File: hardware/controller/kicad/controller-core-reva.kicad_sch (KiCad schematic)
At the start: 187 parts, among them J101 12V_ISOLATED_INPUT / JST XH, J102 STM_SWD / 1x6 2.54mm, J103 ESP_UART / 1x6 2.54mm, J104 UI_LINK / IDC 2x8 2.54mm, J105 JP13 NTC / 2 vías, J106 JP5 FLOW ADAPTER / VCC-GND-OC, J107 JP14 DOOR / contacto seco, J108 JP16 VISUAL V1..V8 / XH-8, J109 JP22 WATER / RED-WHITE-BLACK, J110 USB-C SERVICE / USB 2.0, J111 USB BENCH POWER / OPEN, J112 24V_ACTUATOR_INPUT / JST XH, J113 JP3 VALVE / JST XH, J114 POWER MONITOR / MEASURE ONLY, J115 JP8 GRINDER / 320VDC, J116 JP19 HEATER / 1900W 27R5, J117 JP24 PUMP / 230VAC, J118 JP17 MAINS / L-N, J119 JP1 PE TO BOILER, J120 JP9 PE INPUT, J121 24V INTERNAL SELECT / OPEN FO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, K701 G5RL-1A-E-TV8 DC24, Q501 SI2308A, Q701 SI2308A / relay coil, Q703 BTA24-800BWRG / heater, Q704 BTA24-800BWRG / pump, Q705 SI2308A / heater opto LED, Q706 SI2308A / pump opto LED, Q707 SI2308A / grinder opto LED, Q708 BTA24-800BWRG / grinder, U101 STM32G431RBT6, U201 ESP32-S3-WROOM-1U-N8R8, U203 USBLC6-2SC6, U301 AP63203WU-7, U302 TPS22918DBVR, U303 AP63200WU-7 / 24V to 12V, U501 DRV8876PWPR, U502 UCC27517DBVR, U601 TPS3828-33DBVR, U602 SN74LVC2G08DCTR, U603 SN74LVC2G08DCTR, U604 SN74LVC2G08DCTR, U701 MOC3083 / zero-cross, U702 MOC3083 / zero-cross, U703 MOC3083 / zero-cross

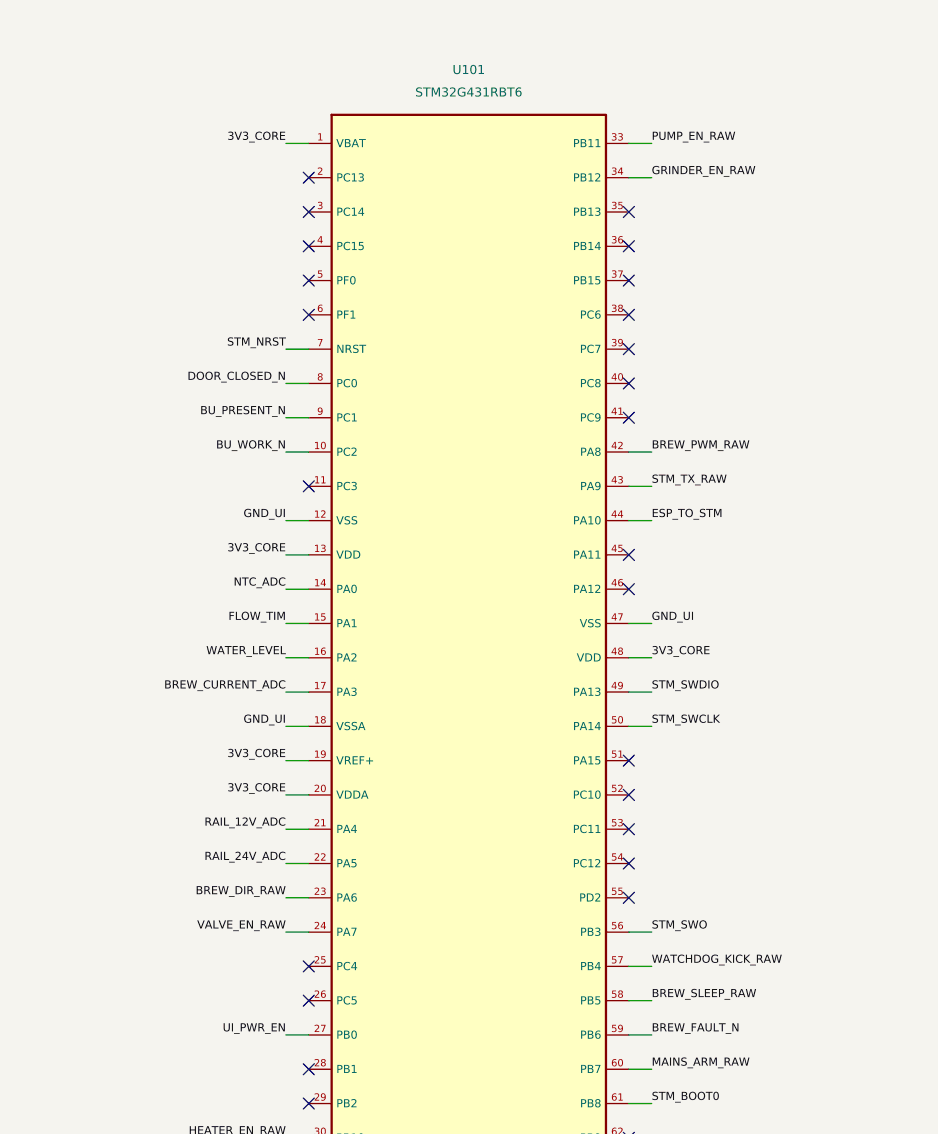
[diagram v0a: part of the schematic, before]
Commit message: Route the load orders and the U602 outputs
Every F.Cu path from the STM32 to the gates west of the 24 V trunk
crosses the reset line, both 24 V branches and the 3.3 V spine; a per-net
search needed 24 to 38 vias for the five nets. The four orders now run as
one bus on B.Cu along the southern edge of the ground plane, two vias
each, at the 0.4 mm pitch that fits between the 3.3 V hop vias and the
barrier. North to south: pump, valve, grinder, heater, which is also the
order in which they peel off west of the trunk.

For that order to hold at the MCU end, GRINDER_EN_RAW moves from PB12 to
PC4, beside PA7 in the south row. PA7, PC4 and PB10 drop into the pocket
under U101 that the decoupling and the pump order fence off on F.Cu, and
come down east of PB11's via. The firmware has no pin map yet.

PB7's hop under the trunk moves north to y = 53.25 mm and the west via of
the 3.3 V hop shifts to x = 44.75 mm to let it down. C602 now shares
R604's ground via: its own sat between two lanes on a piece of plane they
cut off. The GND_UI fill keeps its six pieces.

U602: reset crosses from pin 6 to pin 2 inside the package, the brew
sleep output climbs beside the watchdog kick to R505.1, and the valve
output runs to R511.1 with one hop under the 24 V branch at y = 91.5 mm.

ERC 0; netlist 187 components / 612 pins. DRC: 0 violations, the
intentional dangling end at PA3, 44 open connections (50 before), all
signals.

Co-Authored-By: Claude Opus 5.5 <noreply@anthropic.com>
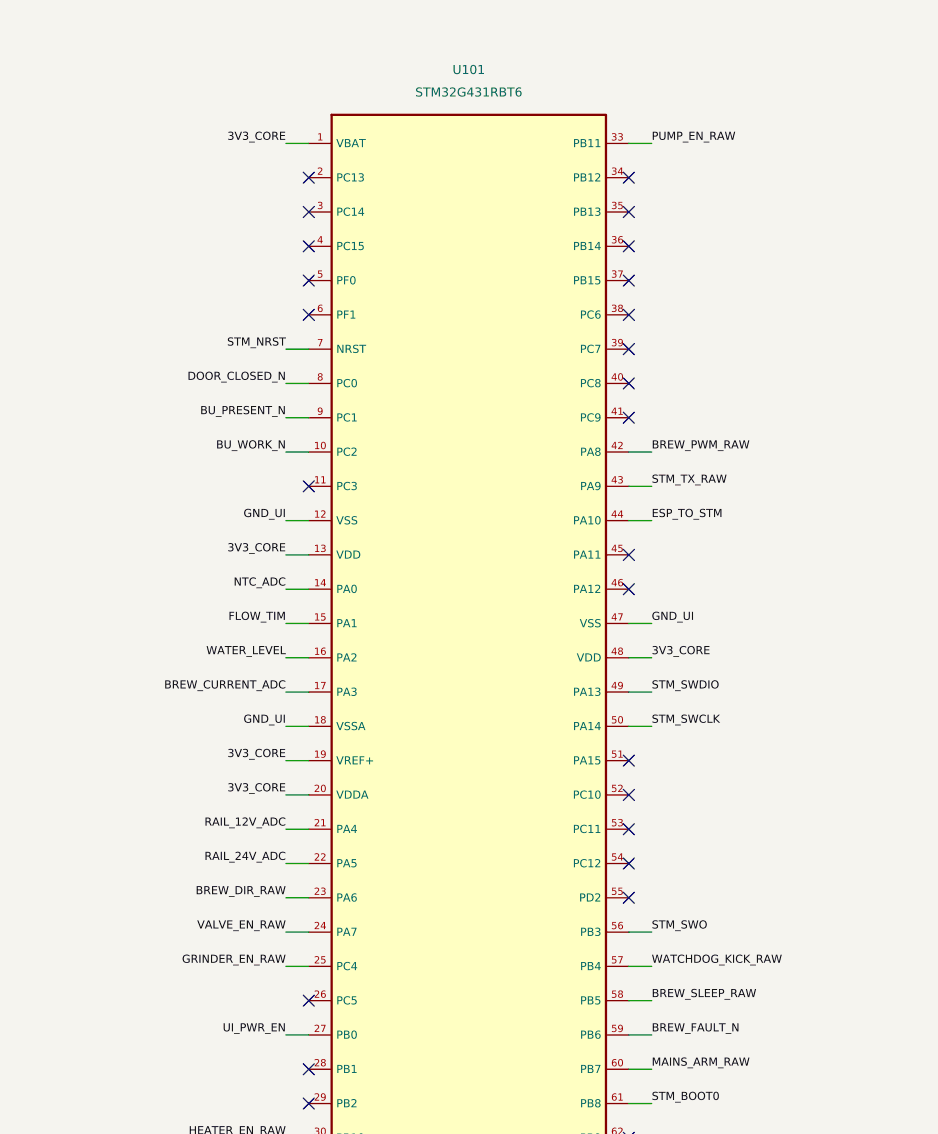
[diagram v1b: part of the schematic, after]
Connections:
- net GRINDER_EN_RAW: now also U101.25 (PC4); no longer U101.34 (PB12)

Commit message: Route the MCU's east side, the H-bridge orders and the rail telemetry
With the firmware still without a pin map, six pins move to where their
nets can leave U101 without crossing:

- UI_PWR_EN PB0 -> PB12 (freed by the grinder order), east of the MCU,
  facing U302.
- BREW_DIR_RAW PA6 -> PC14, BREW_PWM_RAW PA8 -> PF0 (TIM1_CH3N) and
  RAIL_12V_ADC PA4 -> PF1 (ADC2_IN10): the top of the west row, which
  opens onto the free band between the supervisor orders and J114.
- BREW_CURRENT_ADC PA3 -> PC0 (ADC12_IN6), DOOR_CLOSED_N PC0 -> PC3.

The alternate functions were checked against the STM32G431RBTx symbol
in the KiCad library.

The 12 V and 24 V dividers move into the empty pocket under J114, which
feeds them from J114.3 and the 24 V branch and takes both outputs. The
12 V one sat in the far north-east corner, and in the old 24 V row
RAIL_24V_DIV was cut off on both layers by the 3.3 V drop to J114.2 and
the mains arm order.

Routed: the UART up the lane left beside J102 to R211/R212, BOOT0 under
the MCU's north-east corner to R102, reset to J102.5, PB12 to U302, the
bridge orders under the supervisor diagonals to R503/R501, the bridge
current up x = 66.4 mm to the IPROPI line, PF1 straight into J114.5 and
PA5 on B.Cu to J114.6.

ERC 0; netlist 187 / 612. DRC: 0 violations and no warnings (the PA3
dangling end is gone), 29 open connections, all sensor and ESP32 /
front-panel signals. The GND_UI fill keeps its six pieces.

Co-Authored-By: Claude Opus 5.5 <noreply@anthropic.com>
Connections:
- net BREW_CURRENT_ADC: now also U101.8 (PC0); no longer U101.17 (PA3)
- net BREW_DIR_RAW: now also U101.3 (PC14); no longer U101.23 (PA6)
- net BREW_PWM_RAW: now also U101.5 (PF0); no longer U101.42 (PA8)
- net DOOR_CLOSED_N: now also U101.11 (PC3); no longer U101.8 (PC0)
- net RAIL_12V_ADC: now also U101.6 (PF1); no longer U101.21 (PA4)
- net UI_PWR_EN: now also U101.34 (PB12); no longer U101.27 (PB0)
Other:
- note added: "PB12 controla UI_PWR_EN; pull-up mantiene el frontal encendido durante reset."
- note added: "PC3: 0=cajón y puerta colocados; 1=abierto. Medido sin tensión."
- note added: "PF0 PWM (TIM1_CH3N), PC14 dirección, PB5 nSLEEP, PB6 nFAULT, PC0 ADC. PMODE/IMODE a GND."
- note added: "PF1=ADC2_IN10, PA5=ADC2_IN13. Divisor 200k/10k: Vin=21×ADC; RC≈0,95ms."
- note removed: "PA4=ADC2_IN17, PA5=ADC2_IN13. Divisor 200k/10k: Vin=21×ADC; RC≈0,95ms."
- note removed: "PA8 PWM, PA6 dirección, PB5 nSLEEP, PB6 nFAULT, PA3 ADC. PMODE/IMODE a GND."
- note removed: "PB0 controla UI_PWR_EN; pull-up mantiene el frontal encendido durante reset."
- note removed: "PC0: 0=cajón y puerta colocados; 1=abierto. Medido sin tensión."

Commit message: Route the sensor inputs as one B.Cu bus and move the 24 V telemetry to PC1
The sensor lanes leave U101 in the order of their filters, so the bus has
no crossings and every net uses two vias:
- PC3 water, PC2 group present, PA0 group at work, PA1 door,
  PA2 flow (TIM2_CH3), PA3 NTC (ADC1_IN4);
- RAIL_24V_ADC moves from PA5 to PC1 (ADC2_IN7) and reaches J114.6 in
  7 mm, which removes the B.Cu lane that fenced the escape pocket.
The brew sleep and watchdog climbs beside the supervisor move to In2.Cu
so the bus crosses that column on B.Cu. Pin 12 no longer ties to C102
by track; both reach the ground plane on their own vias.
DRC 0 violations; 23 open connections, all ESP32 and front panel.

Co-Authored-By: Claude Opus 5.5 <noreply@anthropic.com>
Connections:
- net BU_PRESENT_N: now also U101.10 (PC2); no longer U101.9 (PC1)
- net BU_WORK_N: now also U101.14 (PA0); no longer U101.10 (PC2)
- net DOOR_CLOSED_N: now also U101.15 (PA1); no longer U101.11 (PC3)
- net FLOW_TIM: now also U101.16 (PA2); no longer U101.15 (PA1)
- net NTC_ADC: now also U101.17 (PA3); no longer U101.14 (PA0)
- net RAIL_24V_ADC: now also U101.9 (PC1); no longer U101.22 (PA5)
- net WATER_LEVEL: now also U101.11 (PC3); no longer U101.16 (PA2)
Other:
- note added: "PA1: 0=cajón y puerta colocados; 1=abierto. Medido sin tensión."
- note added: "PA2 TIM2_CH3. Pin 1 señal, 2 GND, 3 VCC; pin 1 es pad cuadrado/izquierda en vista cenital."
- note added: "PA3 ADC1_IN4. NTC a masa; abierto≈3V3, corto≈0V. Usar tabla del manual."
- note added: "PC2 (presencia) / PA0 (trabajo) activos a 0. V1 rojo=OUT1, V2 azul=OUT2, V3/V4 puente,"
- note added: "PC3 ADC12_IN9/GPIO. Pin 1 rojo=3V3, 2 blanco=señal, 3 negro=GND; salida por caracterizar."
- note added: "PF1=ADC2_IN10, PC1=ADC2_IN7. Divisor 200k/10k: Vin=21×ADC; RC≈0,95ms."
- note removed: "PA0 ADC1_IN1. NTC a masa; abierto≈3V3, corto≈0V. Usar tabla del manual."
- note removed: "PA1 TIM2_CH2. Pin 1 señal, 2 GND, 3 VCC; pin 1 es pad cuadrado/izquierda en vista cenital."
- note removed: "PA2 ADC1_IN3/GPIO. Pin 1 rojo=3V3, 2 blanco=señal, 3 negro=GND; salida por caracterizar."
- note removed: "PC1/PC2 activos a 0. V1 rojo=OUT1, V2 azul=OUT2, V3/V4 puente,"
- note removed: "PC3: 0=cajón y puerta colocados; 1=abierto. Medido sin tensión."
- note removed: "PF1=ADC2_IN10, PA5=ADC2_IN13. Divisor 200k/10k: Vin=21×ADC; RC≈0,95ms."

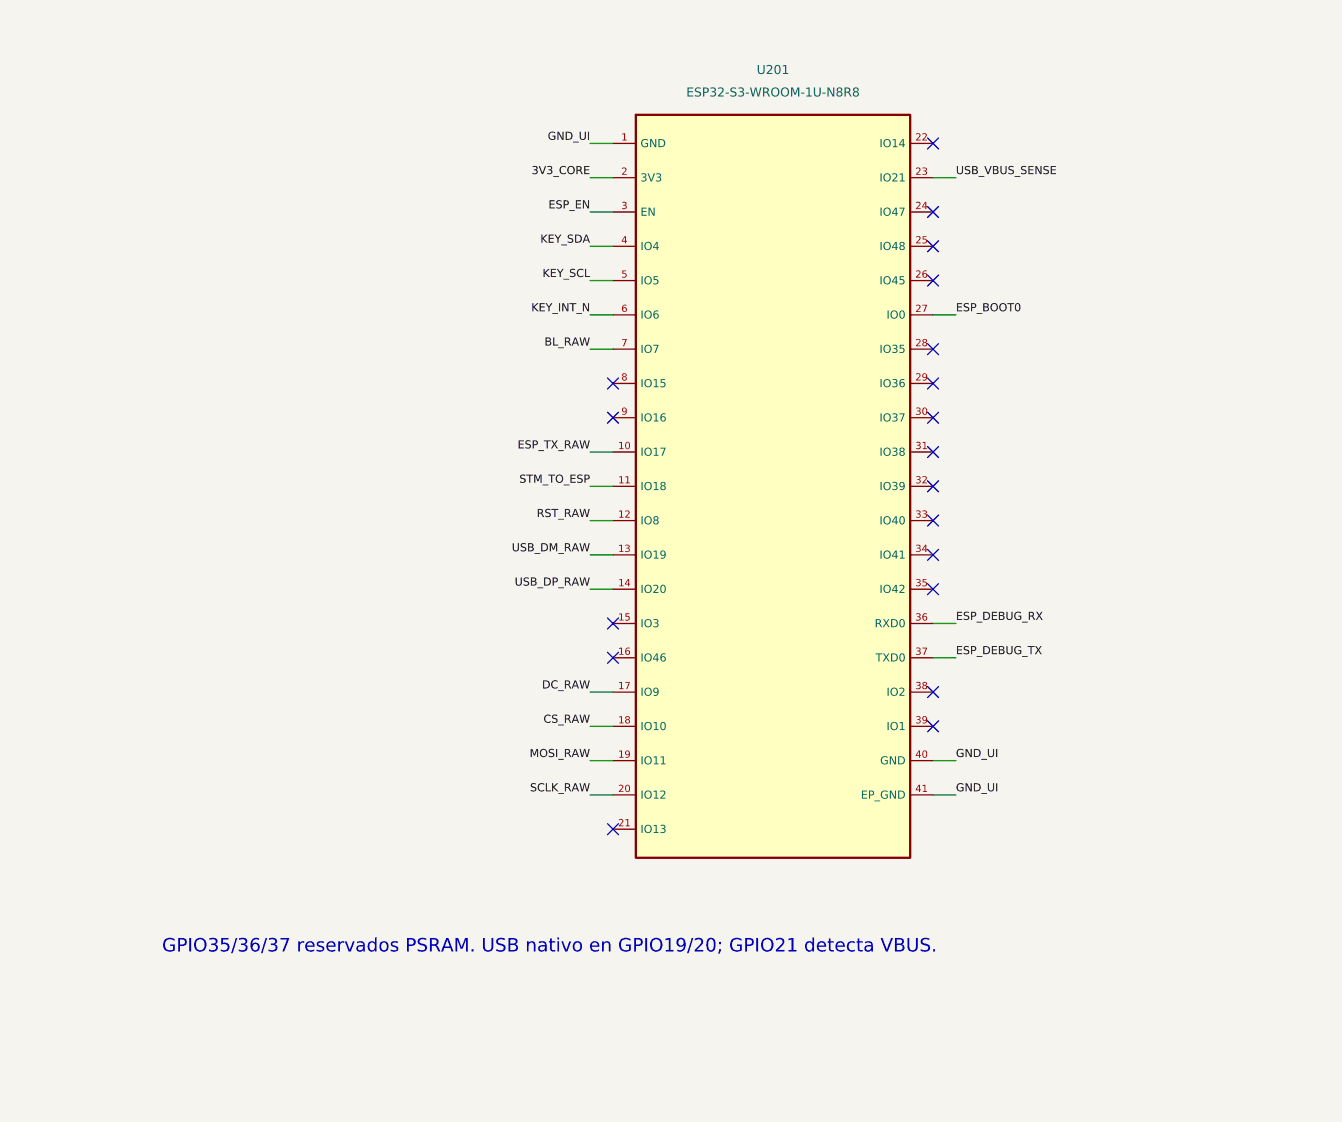
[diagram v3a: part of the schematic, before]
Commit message: Route the ESP32 and front-panel signals; every net is now connected
- R213-R218 move to one row under J104, at the cable entry, in the order
  the bus arrives: the LCD lines reach it without crossings, the four SPI
  lines as a parallel B.Cu bus with no vias beyond their ends.
- ESP UART moves to east-side pins (TX IO17->IO42, RX IO18->IO2) beside
  R211/R212, so it no longer crosses under the module.
- VBUS sense moves from IO21 to IO15, next to its divider; the 30 mm
  line under the module's south row is gone.
- Keypad, EN, debug header and BOOT0 routed; nothing on F.Cu under the
  module and no via in a pad.
DRC 0 violations and 0 unconnected items; parity differences are only
the mounting holes.

Co-Authored-By: Claude Opus 5.5 <noreply@anthropic.com>
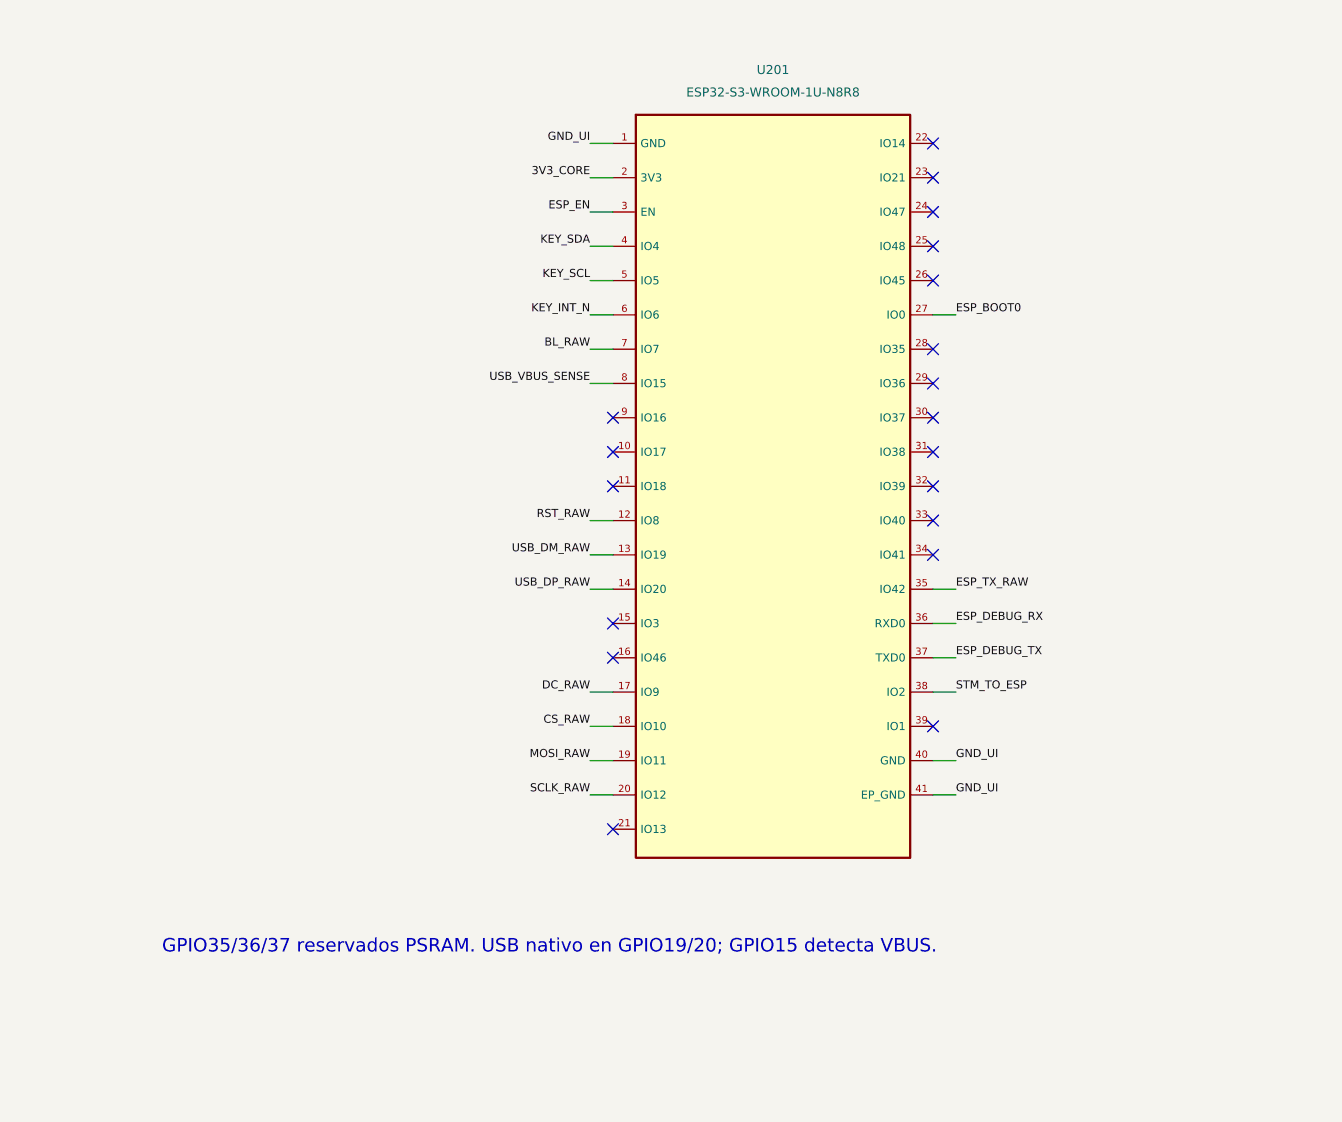
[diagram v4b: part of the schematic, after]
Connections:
- net ESP_TX_RAW: now also U201.35 (IO42); no longer U201.10 (IO17)
- net STM_TO_ESP: now also U201.38 (IO2); no longer U201.11 (IO18)
- net USB_VBUS_SENSE: now also U201.8 (IO15); no longer U201.23 (IO21)
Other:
- note added: "GPIO35/36/37 reservados PSRAM. USB nativo en GPIO19/20; GPIO15 detecta VBUS."
- note removed: "GPIO35/36/37 reservados PSRAM. USB nativo en GPIO19/20; GPIO21 detecta VBUS."

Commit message: Size the grinder for 3 A and double the load phase under the heatsink
On the owner's call the grinder stage is sized for 3 A instead of an
assumed 1 A running current. 3 A is not a credible running current with a
68 ohm winding (it would burn about 610 W in the copper); it is an envelope
close to the 3.4 A stall, so no part depends on the measurement any more.
F703 becomes a JDT JFC2410-1400TS, T4A (C136386, 19,798 in stock), on the
same footprint: 75 % loaded at 3 A. It no longer cuts a stall, which is the
firmware's job. BR701 stays a KBP410: at 3 A it dissipates about 5 W, so it
is rated for grinds of up to 10 s with a pause; a GBU does not fit between
the barrier and JP19. The grinder tracks widen to 1.9 mm into the fuse and
1.2 mm after it, about 12 K at 3 A.

The switched load phase was a single F.Cu run from the lane to the heater
triac: 1.5 mm along the strip and 0.9 mm into Q703, about 90 K and over
150 K at 8.4 A by IPC-2221. It could not be doubled because the heater
gate ran underneath it on B.Cu. The heatsink-foot keepout now covers F.Cu
and the inner layers only, and B.Cu under the foot carries an 18 x 19 mm
block of the phase, stitched by 13 vias. The lane goes to 3.3 mm, the strip
to 1.7 mm, the triac drops to 1.9 mm and the heater output to 3 mm. The
heater gate crosses under the lane at y = 85.6 mm and drops to Q703 east of
the block.

Heater 8.4 A plus grinder 3 A plus pump would draw 11.6 A through F701 and
JP17. While the grinder runs, the heater now conducts at most 3 whole
cycles in 5, leaving about 9.7 A; each grind lasts at most 10 s. The rule
is in the C core as osc_heater_cycles_allowed(), with a CTest check.

ERC 0, netlist 187 components / 612 pins. DRC with all severities: no
violations, no open connections and the three mounting-hole parity entries.

Co-Authored-By: Claude Opus 5.5 <noreply@anthropic.com>
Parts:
- F703: value T2A / 250V grinder -> T4A / 250V grinder; lcsc C136382 -> C136386; mpn JFC2410-1200TS -> JFC2410-1400TS
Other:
- note added: "18 / Etapa del molinillo — V3.2, 68 ohm, 320 V DC; dimensionada a 3 A"
- note added: "BR701 KBP410 4 A / 1 kV, RthJA 55 C/W: ~5 W a 3 A, solo molido intermitente (<=10 s y pausa). Medir en el prototipo."
- note added: "Q708 en el perfil del calentador y la bomba: ~2,5 W a 3 A. Bloqueo = 230/68 = 3,4 A ef.: lo corta el firmware; F703 T4A cubre cortos."
- note removed: "18 / Etapa del molinillo — V3.2, 68 ohm, 320 V DC; 1 A supuesto"
- note removed: "BR701 KBP410 4 A / 1 kV, RthJA 55 C/W: ~1,7 W y +95 K a 1 A continuo; el molido es intermitente. Medir en el prototipo."
- note removed: "Q708 en el perfil del calentador y la bomba: ~0,8 W a 1 A. Bloqueo = 230/68 = 3,4 A ef.: lo corta el firmware; F703 T2A cubre cortos."
